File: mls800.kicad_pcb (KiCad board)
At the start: 2 copper layers, 293.4 x 80.5 mm, 106 parts, among them CON1 BARREL_JACK, IC1 6N137, J1 USB, J10 NSJ8HC, J11 NRJ4HF-1, J2 NRJ4HF-1, J3 NSJ8HC, J4 NSJ8HC, J5 NSJ8HC, J6 NSJ8HC, J7 NSJ8HC, J8 NSJ8HC, J9 NSJ8HC, P1 CONN_02X03, P2 DIN_5, P3 DIN_5, P4 CONN_02X03, P5 CONN_02X03, SW10 SW_TACT_LED, SW11 SW_TACT_LED, SW12 SW_PUSH_RIGHT_ANGLE, SW2 SW_TACT_LED, SW3 SW_TACT_LED, SW4 SW_TACT_LED, SW5 SW_TACT_LED, SW6 SW_TACT_LED, SW7 SW_TACT_LED, SW8 SW_TACT_LED, SW9 SW_TACT_LED, U1 LM340MP-5.0/NOPB, U2 ATmega32U4-AU, U3 24LC256, U4 MCP23017, U5 AS1115, U6 ULN2803A, U7 ULN2803A, U8 LM340MP-5.0/NOPB, X1 16Mhz

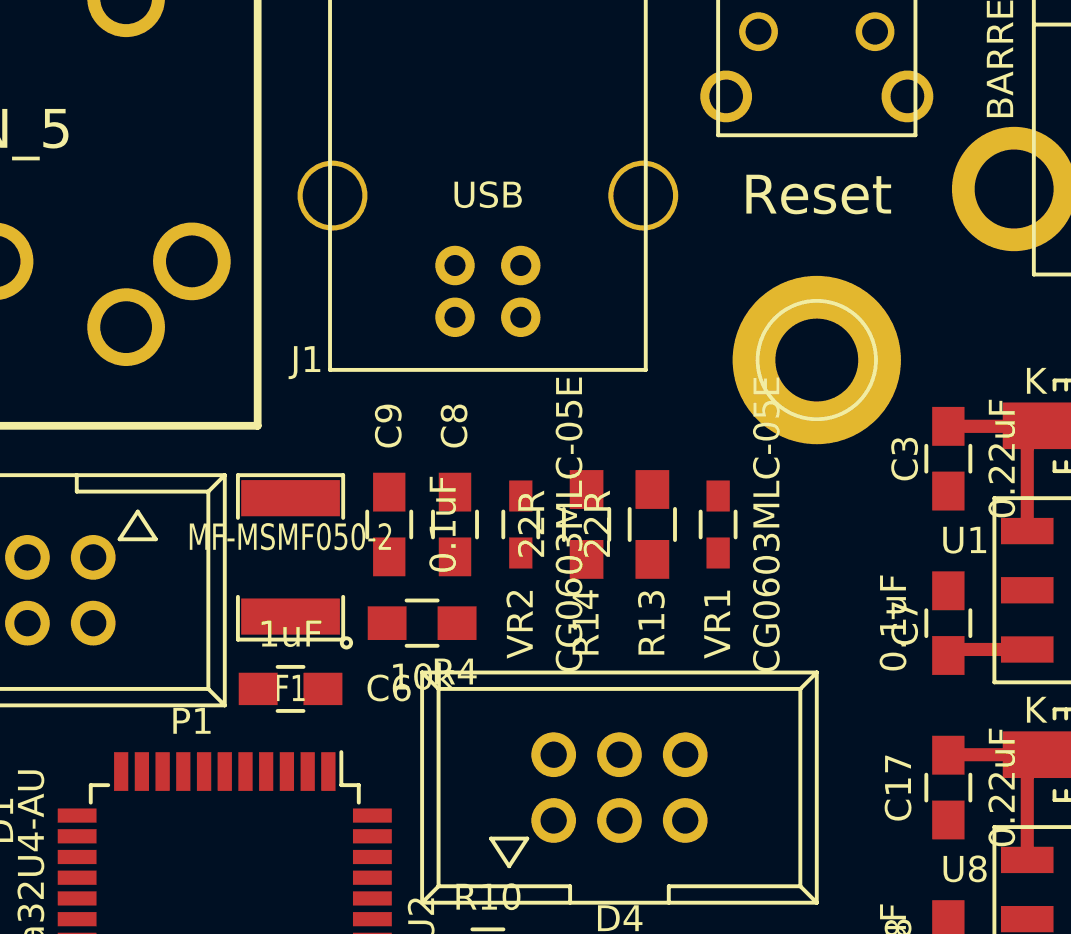
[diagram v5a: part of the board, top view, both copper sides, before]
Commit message: usb port power and data routing
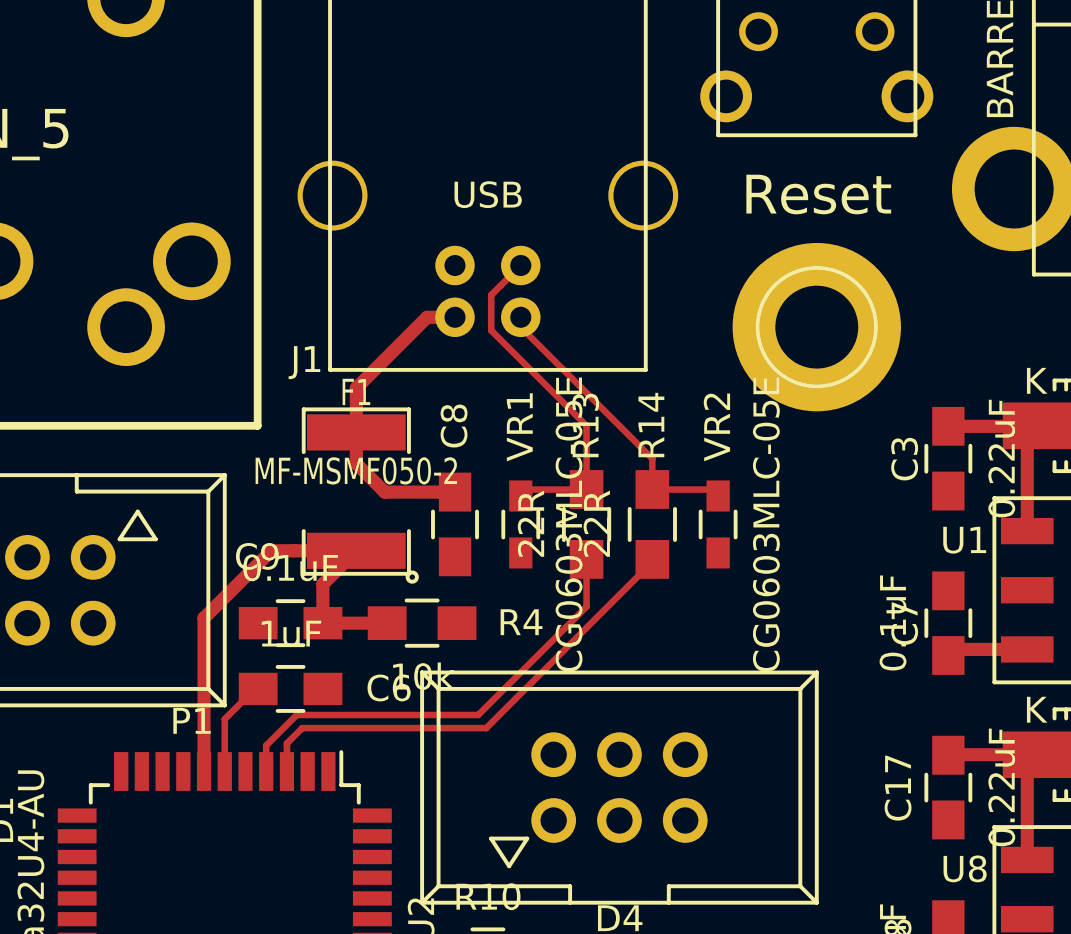
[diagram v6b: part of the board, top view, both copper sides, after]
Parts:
- moved VR1 7.62 mm to (293.4, 68.6)
- moved VR2 7.62 mm to (301.0, 68.6)
- moved C9 5.39 mm to (284.5, 72.4), turned to 180 degrees
- moved F1 3.59 mm to (287.0, 67.3)
- moved R13 2.54 mm to (295.9, 68.6)
- moved R14 2.54 mm to (298.4, 68.6)
- moved MH 1.27 mm to (304.8, 61.0)
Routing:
- net VCOM: track 0.00 -> 18.7 mm
- net /D-: track 0.00 -> 18.2 mm
- net /D+: track 0.00 -> 17.4 mm
- net Net-(J1-Pad3): track 0.49 -> 13.8 mm
- net Net-(C8-Pad1): track 0.00 -> 12.1 mm
- net Net-(J1-Pad2): track 0.00 -> 11.4 mm
- net Net-(RE4-Pad9): track 2.33 -> 7.19 mm
- net Net-(RE3-Pad9): track 15.8 -> 10.9 mm
- net Net-(C6-Pad2): track 0.00 -> 3.80 mm

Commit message: move some parts around usb routing
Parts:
- moved P4 36.1 mm to (262.9, 90.2), turned to 180 degrees
- moved C14 16.2 mm to (298.4, 82.5)
- moved R6 15.3 mm to (298.4, 87.6)
- moved C15 14.5 mm to (303.5, 85.1)
- moved D3 11.7 mm to (304.8, 78.7)
- moved D4 11.7 mm to (304.8, 76.2)
- moved R10 11.7 mm to (299.7, 76.2), turned to 180 degrees
- moved R9 11.7 mm to (299.7, 78.7), turned to 180 degrees
- moved C2 10.9 mm to (274.3, 78.7)
- moved X1 9.92 mm to (278.1, 83.8)
- moved C1 8.98 mm to (274.3, 88.9)
- moved C9 8.03 mm to (292.1, 69.8), turned to 0 degrees
- moved C6 7.62 mm to (292.1, 74.9)
- moved C20 6.99 mm to (230.5, 87.6)
- moved U2 6.35 mm to (288.3, 83.8)
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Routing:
- net VCC: track 44.0 -> 96.5 mm
- net Net-(D5-Pad1): track 0.00 -> 29.3 mm
- net /MISO: track 0.00 -> 19.6 mm
- net Net-(P2-Pad4): track 1.45 -> 15.6 mm
- net /SCK: track 0.00 -> 13.0 mm
- net Net-(D5-Pad2): track 0.25 -> 12.9 mm
- net Net-(C1-Pad2): track 0.00 -> 12.6 mm
- net /RESET: track 0.00 -> 12.1 mm
- net Net-(C2-Pad2): track 0.00 -> 11.9 mm
- net /MOSI: track 0.00 -> 11.2 mm
- net /Loops/SDA: track 5.21 -> 14.3 mm
- net /Loops/SCL: track 7.87 -> 17.0 mm
- net Net-(R6-Pad2): track 0.00 -> 7.56 mm
- net Net-(RE4-Pad9): track 7.19 -> 2.33 mm
- net Net-(RE3-Pad9): track 10.9 -> 15.8 mm
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
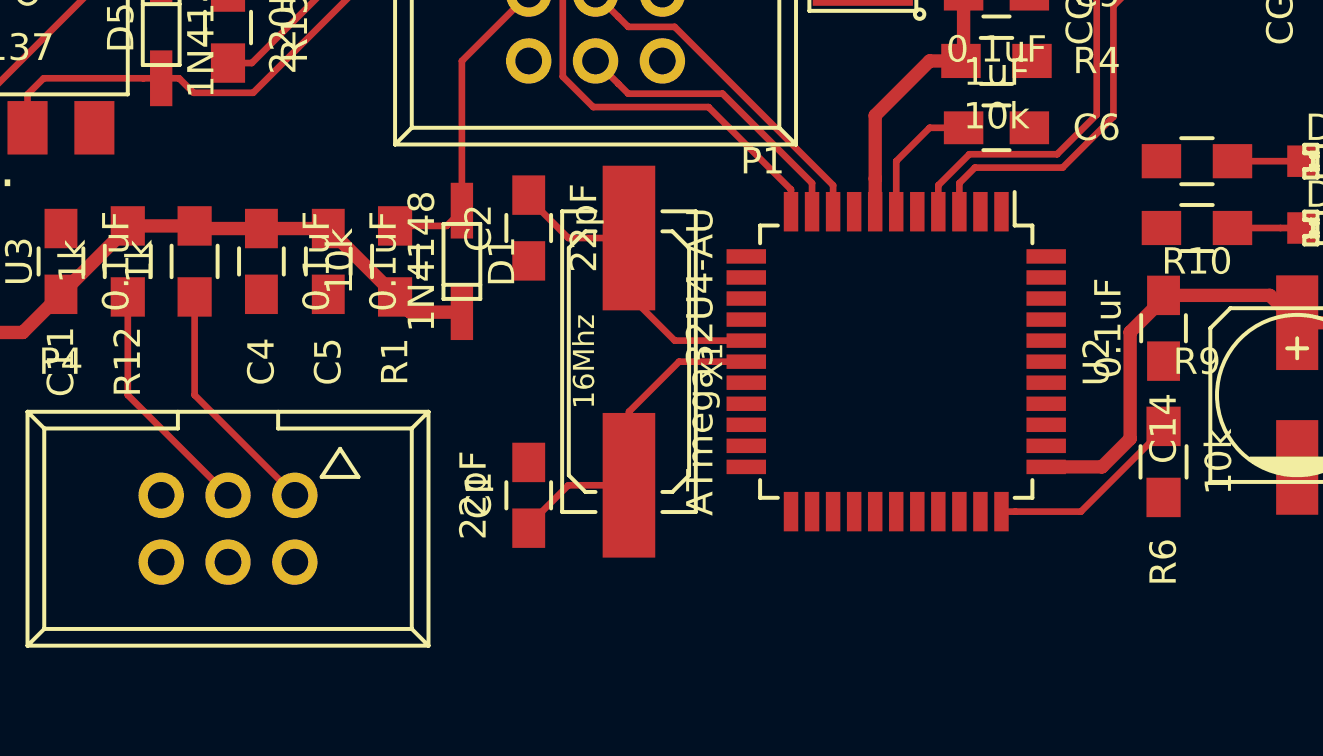
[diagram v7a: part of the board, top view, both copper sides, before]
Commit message: Routing of front panel connector
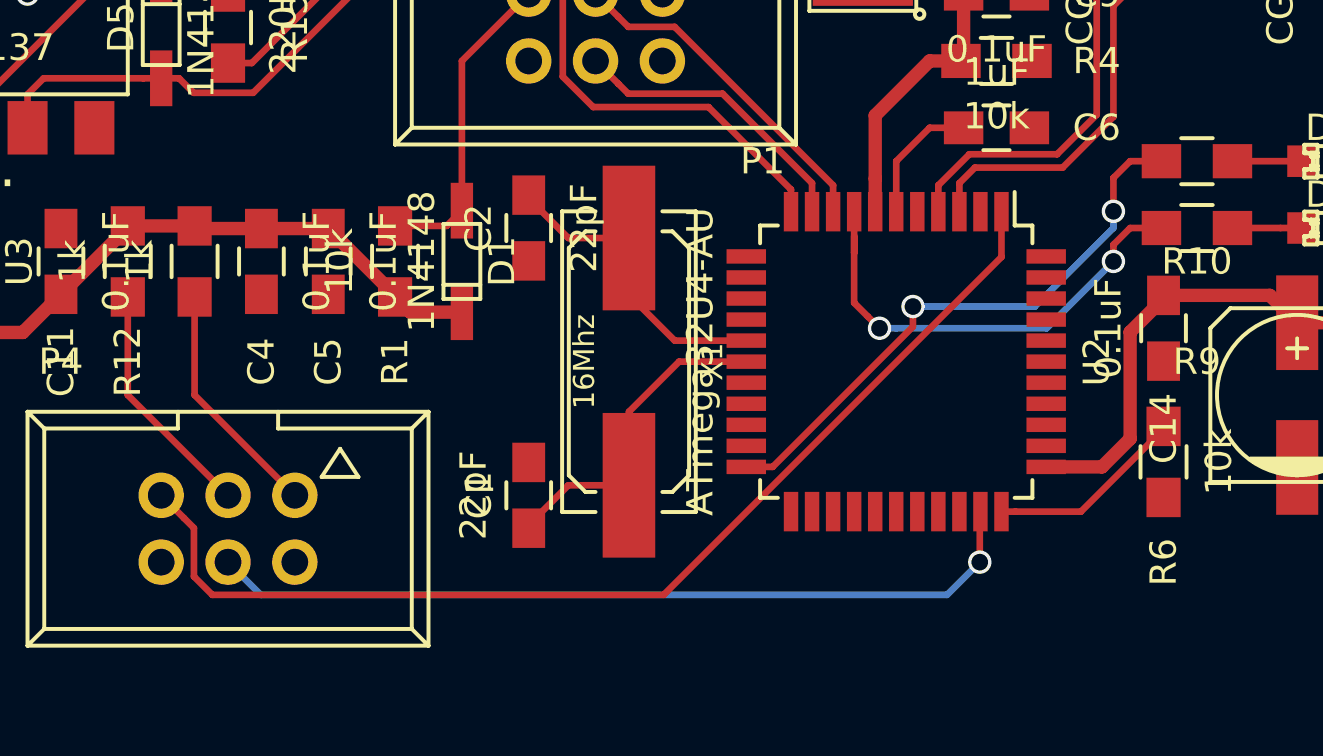
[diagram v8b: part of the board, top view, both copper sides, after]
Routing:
- net /UI_INT: track 0.00 -> 41.6 mm
- net /EDIT_LED: track 0.00 -> 31.5 mm, vias 0 -> 1
- net /TXLED: track 0.00 -> 22.2 mm, vias 0 -> 2
- net /RXLED: track 0.00 -> 18.1 mm, vias 0 -> 2
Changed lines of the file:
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@@
   (general
     (links 345)
-    (no_connects 104)
+    (no_connects 99)
     (area 29.159999 31.440001 350.9 142.1)
     (thickness 1.6)
     (drawings 31)
-    (tracks 963)
+    (tracks 1000)
     (zones 0)
     (modules 106)
@@
   (segment (start 216.944999 64.343001) (end 217.326001 63.961999) (width 0.254) (layer F.Cu) (net 37))
   (segment (start 278.536401 68.986401) (end 279.4 69.85) (width 0.254) (layer F.Cu) (net 38))
+  (segment (start 278.155399 68.605399) (end 278.536401 68.986401) (width 0.254) (layer F.Cu) (net 38))
   (segment (start 276.262591 68.605399) (end 278.155399 68.605399) (width 0.254) (layer F.Cu) (net 38))
   (segment (start 275.615399 69.252591) (end 276.262591 68.605399) (width 0.254) (layer F.Cu) (net 38))
@@
   (segment (start 276.770601 74.142611) (end 275.615399 72.987409) (width 0.254) (layer F.Cu) (net 38))
   (segment (start 281.152611 74.142611) (end 276.770601 74.142611) (width 0.254) (layer F.Cu) (net 38))
-  (segment (start 278.155399 68.605399) (end 278.536401 68.986401) (width 0.254) (layer F.Cu) (net 38))
   (segment (start 284.29 77.28) (end 281.152611 74.142611) (width 0.254) (layer F.Cu) (net 38))
   (segment (start 284.29 78.12) (end 284.29 77.28) (width 0.254) (layer F.Cu) (net 38))
-  (segment (start 277.723599 70.713599) (end 276.86 69.85) (width 0.254) (layer F.Cu) (net 39))
-  (segment (start 278.104601 71.094601) (end 277.723599 70.713599) (width 0.254) (layer F.Cu) (net 39))
-  (segment (start 279.868601 71.094601) (end 278.104601 71.094601) (width 0.254) (layer F.Cu) (net 39))
-  (segment (start 285.89 77.116) (end 279.868601 71.094601) (width 0.254) (layer F.Cu) (net 39))
   (segment (start 285.89 78.12) (end 285.89 77.116) (width 0.254) (layer F.Cu) (net 39))
+  (segment (start 285.89 77.116) (end 279.868601 71.094601) (width 0.254) (layer F.Cu) (net 39))
+  (segment (start 279.868601 71.094601) (end 278.104601 71.094601) (width 0.254) (layer F.Cu) (net 39))
+  (segment (start 278.104601 71.094601) (end 277.723599 70.713599) (width 0.254) (layer F.Cu) (net 39))
+  (segment (start 277.723599 70.713599) (end 276.86 69.85) (width 0.254) (layer F.Cu) (net 39))
   (segment (start 277.723599 73.253599) (end 276.86 72.39) (width 0.254) (layer F.Cu) (net 40))
   (segment (start 278.104601 73.634601) (end 277.723599 73.253599) (width 0.254) (layer F.Cu) (net 40))
@@
   (segment (start 91.44 116.686) (end 91.34 116.586) (width 0.254) (layer F.Cu) (net 54))
   (segment (start 91.44 119.046) (end 91.44 116.686) (width 0.254) (layer F.Cu) (net 54))
+  (segment (start 288.283617 82.55) (end 287.655 82.55) (width 0.254) (layer B.Cu) (net 55))
+  (segment (start 294.005 82.55) (end 288.283617 82.55) (width 0.254) (layer B.Cu) (net 55))
+  (segment (start 296.545 80.01) (end 294.005 82.55) (width 0.254) (layer B.Cu) (net 55))
+  (segment (start 287.210501 82.105501) (end 287.655 82.55) (width 0.254) (layer F.Cu) (net 55))
+  (segment (start 286.69 81.585) (end 287.210501 82.105501) (width 0.254) (layer F.Cu) (net 55))
+  (segment (start 286.69 79.68) (end 286.69 81.585) (width 0.254) (layer F.Cu) (net 55))
+  (via (at 287.655 82.55) (size 0.889) (drill 0.635) (layers F.Cu B.Cu) (net 55))
+  (segment (start 286.69 78.12) (end 286.69 79.68) (width 0.254) (layer F.Cu) (net 55))
+  (segment (start 286.69 79.045) (end 286.69 79.68) (width 0.254) (layer F.Cu) (net 55))
+  (segment (start 296.545 79.375) (end 297.18 78.74) (width 0.254) (layer F.Cu) (net 55))
+  (segment (start 297.18 78.74) (end 298.37 78.74) (width 0.254) (layer F.Cu) (net 55))
+  (segment (start 296.545 80.01) (end 296.545 79.375) (width 0.254) (layer F.Cu) (net 55))
+  (via (at 296.545 80.01) (size 0.889) (drill 0.635) (layers F.Cu B.Cu) (net 55))
+  (segment (start 296.545 76.835) (end 297.18 76.2) (width 0.254) (layer F.Cu) (net 56))
+  (segment (start 297.18 76.2) (end 298.37 76.2) (width 0.254) (layer F.Cu) (net 56))
+  (segment (start 296.545 78.105) (end 296.545 76.835) (width 0.254) (layer F.Cu) (net 56))
+  (segment (start 293.56051 81.72449) (end 296.545 78.74) (width 0.254) (layer B.Cu) (net 56))
+  (segment (start 296.545 78.74) (end 296.545 78.105) (width 0.254) (layer B.Cu) (net 56))
+  (via (at 296.545 78.105) (size 0.889) (drill 0.635) (layers F.Cu B.Cu) (net 56))
+  (segment (start 288.925 81.72449) (end 293.56051 81.72449) (width 0.254) (layer B.Cu) (net 56))
+  (segment (start 282.59 87.82) (end 283.594 87.82) (width 0.254) (layer F.Cu) (net 56))
+  (segment (start 283.594 87.82) (end 288.925 82.489) (width 0.254) (layer F.Cu) (net 56))
+  (segment (start 288.925 82.489) (end 288.925 81.72449) (width 0.254) (layer F.Cu) (net 56))
+  (via (at 288.925 81.72449) (size 0.889) (drill 0.635) (layers F.Cu B.Cu) (net 56))
   (segment (start 295.91 68.394) (end 295.91 67.39) (width 0.254) (layer F.Cu) (net 57))
   (segment (start 295.91 74.430802) (end 295.91 68.394) (width 0.254) (layer F.Cu) (net 57))
@@
   (segment (start 174.498 121.666) (end 175.768 120.396) (width 0.254) (layer F.Cu) (net 82))
   (segment (start 161.29 121.666) (end 174.498 121.666) (width 0.254) (layer F.Cu) (net 82))
+  (segment (start 291.465 91.44) (end 291.465 89.545) (width 0.254) (layer F.Cu) (net 83))
+  (segment (start 291.465 89.545) (end 291.49 89.52) (width 0.254) (layer F.Cu) (net 83))
+  (segment (start 262.89 91.44) (end 264.134601 92.684601) (width 0.254) (layer B.Cu) (net 83))
+  (segment (start 264.134601 92.684601) (end 290.220399 92.684601) (width 0.254) (layer B.Cu) (net 83))
+  (segment (start 290.220399 92.684601) (end 291.465 91.44) (width 0.254) (layer B.Cu) (net 83))
+  (via (at 291.465 91.44) (size 0.889) (drill 0.635) (layers F.Cu B.Cu) (net 83))
+  (segment (start 292.29 78.12) (end 292.29 79.842434) (width 0.254) (layer F.Cu) (net 84))
+  (segment (start 292.29 79.842434) (end 279.447833 92.684601) (width 0.254) (layer F.Cu) (net 84))
+  (segment (start 279.447833 92.684601) (end 262.292591 92.684601) (width 0.254) (layer F.Cu) (net 84))
+  (segment (start 262.292591 92.684601) (end 261.594601 91.986611) (width 0.254) (layer F.Cu) (net 84))
+  (segment (start 261.594601 91.986611) (end 261.594601 90.144601) (width 0.254) (layer F.Cu) (net 84))
+  (segment (start 261.594601 90.144601) (end 261.213599 89.763599) (width 0.254) (layer F.Cu) (net 84))
+  (segment (start 261.213599 89.763599) (end 260.35 88.9) (width 0.254) (layer F.Cu) (net 84))
   (segment (start 162.2425 109.776) (end 162.73498 109.28352) (width 0.254) (layer F.Cu) (net 85))
   (segment (start 162.73498 109.28352) (end 163.068 109.28352) (width 0.254) (layer F.Cu) (net 85))
